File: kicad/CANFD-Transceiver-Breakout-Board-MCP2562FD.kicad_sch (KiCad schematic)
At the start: 15 parts, among them IC1 MCP2562FD-E_SN, K1 HEADER_MALE_6X1, K2 HEADER_MALE_6X1, K3 TERMINAL_KF235-5.0-2P, U3 ATA6561-GAQW-N

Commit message: editing schematic
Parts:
- removed C6: 100n, e-radionica.com footprinti:0603C, symbol e-radionica.com schematics:0603C
- removed U3: ATA6561-GAQW-N, e-radionica.com footprinti:SOIC−8, symbol e-radionica.com schematics:ATA6561-GAQW-N
- added C2: 100n, e-radionica.com footprinti:0603C, symbol e-radionica.com schematics:0603C
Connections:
- net 3V3: now also C1.2
- net 5V: now also C2.1
- net GND: now also C1.1, C2.2
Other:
- note added: "The device may be placed in Standby mode by applying high-level voltage to the STBY pin."

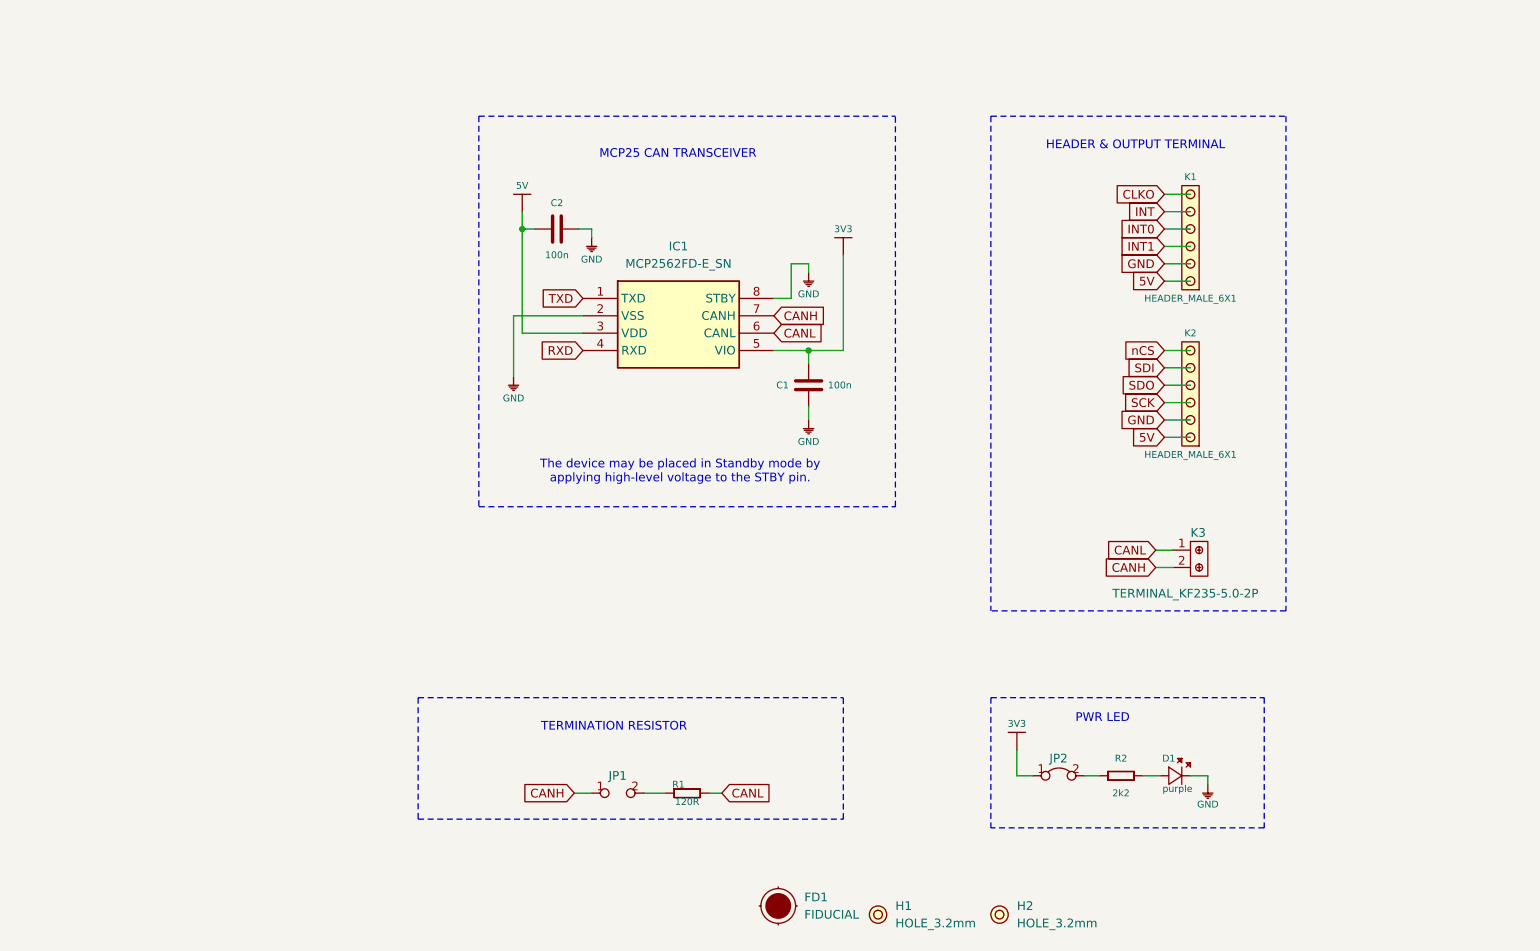
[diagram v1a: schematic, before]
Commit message: finished designing CANFD breakout
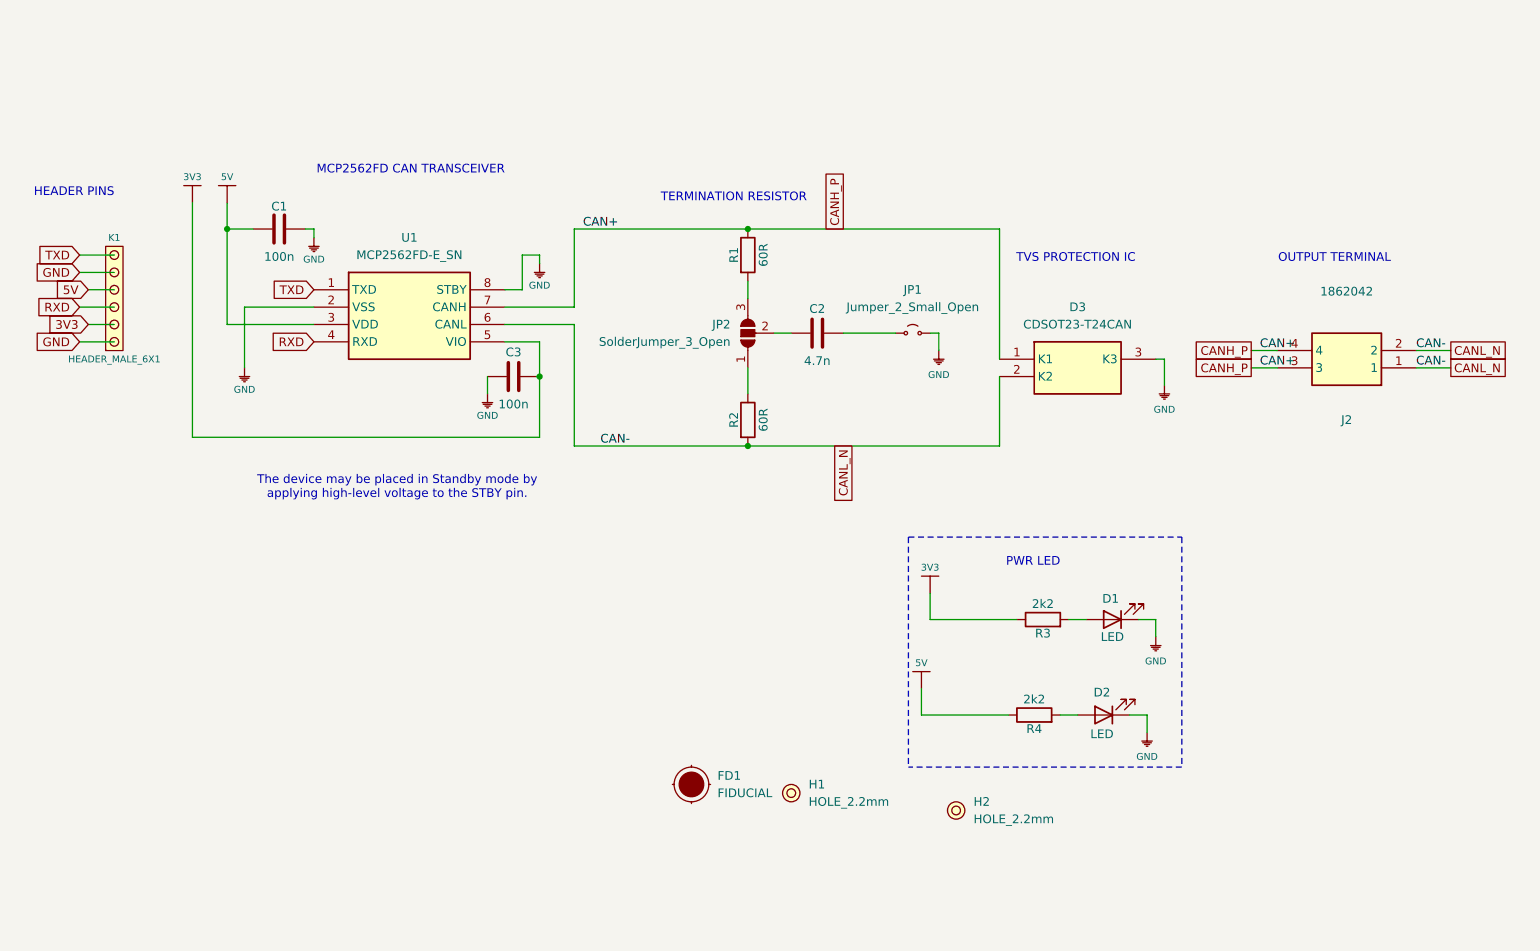
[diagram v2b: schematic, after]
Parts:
- removed C1, C2: 100n, e-radionica.com footprinti:0603C, symbol e-radionica.com schematics:0603C
- removed D1: purple, e-radionica.com footprinti:0402LED, symbol e-radionica.com schematics:0402LED
- removed JP1: SMD_JUMPER, e-radionica.com footprinti:SMD_JUMPER, symbol e-radionica.com schematics:SMD_JUMPER
- removed JP2: SMD-JUMPER-CONNECTED_TRACE_SLODERMASK, e-radionica.com footprinti:SMD-JUMPER-CONNECTED_TRACE_SLODERMASK, symbol e-radionica.com schematics:SMD-JUMPER-CONNECTED_TRACE_SLODERMASK
- removed K2: HEADER_MALE_6X1, e-radionica.com footprinti:HEADER_MALE_6X1, symbol e-radionica.com schematics:HEADER_MALE_6X1
- removed K3: TERMINAL_KF235-5.0-2P, e-radionica.com footprinti:TERMINAL_KF235-5.0-2P, symbol e-radionica.com schematics:TERMINAL_KF235-5.0-2P
- removed R1: 120R, e-radionica.com footprinti:0603R, symbol e-radionica.com schematics:0603R
- removed R2: 2k2, e-radionica.com footprinti:0402R, symbol e-radionica.com schematics:0402R
- added C1, C3: 100n, Capacitor_SMD:C_0603_1608Metric_Pad1.08x0.95mm_HandSolder, symbol Device:C
- added C2: 4.7n, Resistor_SMD:R_0402_1005Metric_Pad0.72x0.64mm_HandSolder, symbol Device:C
- added D1, D2: LED, LED_SMD:LED_0603_1608Metric_Pad1.05x0.95mm_HandSolder, symbol Device:LED
- added D3: CDSOT23-T24CAN, CanFD-Transceiver-FP-Lib:SOT95P230X117-3N, symbol CANFD-Transceiver:CDSOT23-T24CAN
- added J2: 1862042, CanFD-Transceiver-FP-Lib:1862042, symbol CANFD-Transceiver:1862042
- added JP1: Jumper_2_Small_Open, Jumper:SolderJumper-2_P1.3mm_Open_RoundedPad1.0x1.5mm, symbol Jumper:Jumper_2_Small_Open
- added JP2: SolderJumper_3_Open, Jumper:SolderJumper-3_P1.3mm_Open_Pad1.0x1.5mm_NumberLabels, symbol Jumper:SolderJumper_3_Open
- added R1, R2: 60R, Resistor_SMD:R_0402_1005Metric_Pad0.72x0.64mm_HandSolder, symbol Device:R
- added R3, R4: 2k2, Resistor_SMD:R_0603_1608Metric_Pad0.98x0.95mm_HandSolder, symbol Device:R
- FD1: footprint e-radionica.com footprinti:FIDUCIAL_23 -> Fiducial:Fiducial_0.5mm_Mask1mm
- H1, H2: value HOLE_3.2mm -> HOLE_2.2mm; footprint e-radionica.com footprinti:HOLE_3.2mm -> MountingHole:MountingHole_2.2mm_M2_DIN965_Pad_TopBottom
- K1: footprint e-radionica.com footprinti:HEADER_MALE_6X1 -> Connector_PinHeader_2.54mm:PinHeader_1x06_P2.54mm_Horizontal
- renumbered IC1 to U1
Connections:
- net CLKO is gone; now on net TXD: K1.6
- net INT is gone; now on net GND: K1.5
- net INT0 is gone; now on net 5V: K1.4
- net INT1 is gone; now on net RXD: K1.3
- net 3V3: now also K1.2, C3.2, R3.1
- net 5V: now also C1.1, R4.1; no longer K1.1
- net GND: now also K1.1, C1.2, C3.1, D1.1 (K), D2.1 (K), D3.3 (K3), JP1.2 (B); no longer K1.2
- net CANH renamed CANH_P
- net CANH_P: now also D3.1 (K1), J2.3, J2.4, R1.1
- net CANL renamed CANL_N
- net CANL_N: now also D3.2 (K2), J2.1, J2.2, R2.2
- new net: D2.2 (A), R4.2
- new net: C2.2, JP1.1 (A)
- new net: D1.2 (A), R3.2
- new net: C2.1, JP2.2 (C)
- new net: JP2.1 (A), R2.1
- new net: JP2.3 (B), R1.2
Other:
- note added: "HEADER PINS"
- note added: "MCP2562FD CAN TRANSCEIVER"
- note added: "OUTPUT TERMINAL"
- note added: "TVS PROTECTION IC"
- note removed: "HEADER & OUTPUT TERMINAL"
- note removed: "MCP25 CAN TRANSCEIVER"
- moved on the sheet: FD1, H1, K1, U1

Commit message: refine
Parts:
- removed H1, H2: HOLE_2.2mm, MountingHole:MountingHole_2.2mm_M2_DIN965_Pad_TopBottom, symbol e-radionica.com schematics:HOLE_3.2mm
- added H1, H3: HOLE_2.2mm, MountingHole:MountingHole_2.2mm_M2_DIN965_Pad_TopBottom, symbol Mechanical:MountingHole_Pad
- FD1: now left out of the parts list
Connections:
- net GND: now also H1.1, H3.1
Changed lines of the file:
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@@
+	)
+	(symbol
+		(lib_name "e-radionica.com schematics:GND_3")
+		(lib_id "e-radionica.com schematics:GND")
+		(at 177.8 152.4 0)
+		(unit 1)
+		(exclude_from_sim no)
+		(in_bom yes)
+		(on_board yes)
+		(dnp no)
+		(property "Reference" "#PWR013"
+			(at 182.245 152.4 0)
+			(effects
+				(font
+					(size 1 1)
+				)
+				(hide yes)
+			)
+		)
+		(property "Value" "GND"
+			(at 177.8 155.956 0)
+			(effects
+				(font
+					(size 1 1)
+				)
+			)
+		)
+		(property "Footprint" ""
+			(at 182.245 148.59 0)
+			(effects
+				(font
+					(size 1 1)
+				)
+				(hide yes)
+			)
+		)
+		(property "Datasheet" ""
+			(at 182.245 148.59 0)
+			(effects
+				(font
+					(size 1 1)
+				)
+				(hide yes)
+			)
+		)
+		(property "Description" ""
+			(at 177.8 152.4 0)
+			(effects
+				(font
+					(size 1.27 1.27)
+				)
+			)
+		)
+		(pin "1"
+		)
+		(instances
+			(project "CANFD-Transceiver-Breakout-Board-MCP2562FD"
+				(path "/802bf3dd-45f4-457b-8e6e-ea2d44622c13"
+					(reference "#PWR013")
+					(unit 1)
+				)
+			)
+		)
 	)
 	(symbol
@@
 	)
 	(symbol
+		(lib_id "Mechanical:MountingHole_Pad")
+		(at 177.8 149.86 0)
+		(unit 1)
+		(exclude_from_sim no)
+		(in_bom no)
+		(on_board yes)
+		(dnp no)
+		(fields_autoplaced yes)
+		(property "Reference" "H3"
+			(at 180.34 147.3199 0)
+			(effects
+				(font
+					(size 1.27 1.27)
+				)
+				(justify left)
+			)
+		)
+		(property "Value" "HOLE_2.2mm"
+			(at 180.34 149.8599 0)
+			(effects
+				(font
+					(size 1.27 1.27)
+				)
+				(justify left)
+			)
+		)
+		(property "Footprint" "MountingHole:MountingHole_2.2mm_M2_DIN965_Pad_TopBottom"
+			(at 177.8 149.86 0)
+			(effects
+				(font
+					(size 1.27 1.27)
+				)
+				(hide yes)
+			)
+		)
+		(property "Datasheet" "~"
+			(at 177.8 149.86 0)
+			(effects
+				(font
+					(size 1.27 1.27)
+				)
+				(hide yes)
+			)
+		)
+		(property "Description" "Mounting Hole with connection"
+			(at 177.8 149.86 0)
+			(effects
+				(font
+					(size 1.27 1.27)
+				)
+				(hide yes)
+			)
+		)
+		(pin "1"
+		)
+		(instances
+			(project "CANFD-Transceiver-Breakout-Board-MCP2562FD"
+				(path "/802bf3dd-45f4-457b-8e6e-ea2d44622c13"
+					(reference "H3")
+					(unit 1)
+				)
+			)
+		)
+	)
+	(symbol
 		(lib_id "Device:C")
 		(at 180.34 68.58 90)
@@
 	)
 	(symbol
+		(lib_name "e-radionica.com schematics:GND_3")
+		(lib_id "e-radionica.com schematics:GND")
+		(at 201.93 152.4 0)
+		(unit 1)
+		(exclude_from_sim no)
+		(in_bom yes)
+		(on_board yes)
+		(dnp no)
+		(property "Reference" "#PWR014"
+			(at 206.375 152.4 0)
+			(effects
+				(font
+					(size 1 1)
+				)
+				(hide yes)
+			)
+		)
+		(property "Value" "GND"
+			(at 201.93 155.956 0)
+			(effects
+				(font
+					(size 1 1)
+				)
+			)
+		)
+		(property "Footprint" ""
+			(at 206.375 148.59 0)
+			(effects
+				(font
+					(size 1 1)
+				)
+				(hide yes)
+			)
+		)
+		(property "Datasheet" ""
+			(at 206.375 148.59 0)
+			(effects
+				(font
+					(size 1 1)
+				)
+				(hide yes)
+			)
+		)
+		(property "Description" ""
+			(at 201.93 152.4 0)
+			(effects
+				(font
+					(size 1.27 1.27)
+				)
+			)
+		)
+		(pin "1"
+		)
+		(instances
+			(project "CANFD-Transceiver-Breakout-Board-MCP2562FD"
+				(path "/802bf3dd-45f4-457b-8e6e-ea2d44622c13"
+					(reference "#PWR014")
+					(unit 1)
+				)
+			)
+		)
+	)
+	(symbol
 		(lib_id "CANFD-Transceiver:MCP2562FD-E_SN")
 		(at 106.68 62.23 0)
@@
 	)
 	(symbol
-		(lib_id "e-radionica.com schematics:HOLE_3.2mm")
-		(at 200.66 138.43 0)
-		(unit 1)
-		(exclude_from_sim no)
-		(in_bom yes)
-		(on_board no)
-		(dnp no)
-		(property "Reference" "H2"
-			(at 203.2 137.16 0)
-			(effects
-				(font
-					(size 1.27 1.27)
-				)
-				(justify left)
-			)
-		)
-		(property "Value" "HOLE_2.2mm"
-			(at 203.2 139.7 0)
-			(effects
-				(font
-					(size 1.27 1.27)
-				)
-				(justify left)
-			)
-		)
-		(property "Footprint" "MountingHole:MountingHole_2.2mm_M2_DIN965_Pad_TopBottom"
-			(at 200.66 138.43 0)
-			(effects
-				(font
-					(size 1.27 1.27)
-				)
-				(hide yes)
-			)
-		)
-		(property "Datasheet" ""
-			(at 200.66 138.43 0)
-			(effects
-				(font
-					(size 1.27 1.27)
-				)
-				(hide yes)
-			)
-		)
-		(property "Description" ""
-			(at 200.66 138.43 0)
-			(effects
-				(font
-					(size 1.27 1.27)
-				)
-			)
-		)
-		(instances
-			(project "CANFD-Transceiver-Breakout-Board-MCP2562FD"
-				(path "/802bf3dd-45f4-457b-8e6e-ea2d44622c13"
-					(reference "H2")
-					(unit 1)
-				)
-			)
-		)
-	)
-	(symbol
 		(lib_id "Device:R")
 		(at 212.09 124.46 90)
@@
 				(path "/802bf3dd-45f4-457b-8e6e-ea2d44622c13"
 					(reference "R4")
+					(unit 1)
+				)
+			)
+		)
+	)
+	(symbol
+		(lib_id "Mechanical:MountingHole_Pad")
+		(at 201.93 149.86 0)
+		(unit 1)
+		(exclude_from_sim no)
+		(in_bom no)
+		(on_board yes)
+		(dnp no)
+		(fields_autoplaced yes)
+		(property "Reference" "H1"
+			(at 204.47 147.3199 0)
+			(effects
+				(font
+					(size 1.27 1.27)
+				)
+				(justify left)
+			)
+		)
+		(property "Value" "HOLE_2.2mm"
+			(at 204.47 149.8599 0)
+			(effects
+				(font
+					(size 1.27 1.27)
+				)
+				(justify left)
+			)
+		)
+		(property "Footprint" "MountingHole:MountingHole_2.2mm_M2_DIN965_Pad_TopBottom"
+			(at 201.93 149.86 0)
+			(effects
+				(font
+					(size 1.27 1.27)
+				)
+				(hide yes)
+			)
+		)
+		(property "Datasheet" "~"
+			(at 201.93 149.86 0)
+			(effects
+				(font
+					(size 1.27 1.27)
+				)
+				(hide yes)
+			)
+		)
+		(property "Description" "Mounting Hole with connection"
+			(at 201.93 149.86 0)
+			(effects
+				(font
+					(size 1.27 1.27)
+				)
+				(hide yes)
+			)
+		)
+		(pin "1"
+		)
+		(instances
+			(project "CANFD-Transceiver-Breakout-Board-MCP2562FD"
+				(path "/802bf3dd-45f4-457b-8e6e-ea2d44622c13"
+					(reference "H1")
 					(unit 1)
 				)
@@
 		(unit 1)
 		(exclude_from_sim no)
-		(in_bom yes)
+		(in_bom no)
 		(on_board no)
 		(dnp no)
@@
 					(unit 1)
 				)
-			)
-		)
-	)
-	(symbol
-		(lib_id "e-radionica.com schematics:HOLE_3.2mm")
-		(at 176.53 135.89 0)
-		(unit 1)
-		(exclude_from_sim no)
-		(in_bom yes)
-		(on_board no)
-		(dnp no)
-		(property "Reference" "H1"
-			(at 179.07 134.62 0)
-			(effects
-				(font
-					(size 1.27 1.27)
-				)
-				(justify left)
-			)
-		)
-		(property "Value" "HOLE_2.2mm"
-			(at 179.07 137.16 0)
-			(effects
-				(font
-					(size 1.27 1.27)
-				)
-				(justify left)
-			)
-		)
-		(property "Footprint" "MountingHole:MountingHole_2.2mm_M2_DIN965_Pad_TopBottom"
-			(at 176.53 135.89 0)
-			(effects
-				(font
-					(size 1.27 1.27)
-				)
-				(hide yes)
-			)
-		)
-		(property "Datasheet" ""
-			(at 176.53 135.89 0)
-			(effects
-				(font
-					(size 1.27 1.27)
-				)
-				(hide yes)
-			)
-		)
-		(property "Description" ""
-			(at 176.53 135.89 0)
-			(effects
-				(font
-					(size 1.27 1.27)
-				)
-			)
-		)
-		(instances
-			(project "CANFD-Transceiver-Breakout-Board-MCP2562FD"
-				(path "/802bf3dd-45f4-457b-8e6e-ea2d44622c13"
-					(reference "H1")
-					(unit 1)
-				)

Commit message: final revision
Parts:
- C1, C3: LCSC_Part_Number (none) -> C16194197; Manufacturer_Name (none) -> Samsung Electro-Mechanics; Manufacturer_Part_Number (none) -> CL10E104KC8VPNC
- C2: LCSC_Part_Number (none) -> C2167398; Manufacturer_Name (none) -> KEMET; Manufacturer_Part_Number (none) -> C0402C472J5RACTU
- D1, D2: LCSC_Part_Number (none) -> C125099; Manufacturer_Name (none) -> LITEON; Manufacturer_Part_Number (none) -> LTST-C191KRKT
- FD1: now not fitted
- J2, JP1, K1: now left out of the parts list
- R1, R2: LCSC_Part_Number (none) -> C274896; Manufacturer_Name (none) -> YAGEO; Manufacturer_Part_Number (none) -> RC0402FR-0762RL
- R3, R4: LCSC_Part_Number (none) -> C114662; Manufacturer_Name (none) -> YAGEO; Manufacturer_Part_Number (none) -> RC0603FR-072K2L
